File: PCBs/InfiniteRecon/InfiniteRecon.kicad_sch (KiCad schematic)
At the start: 0 parts

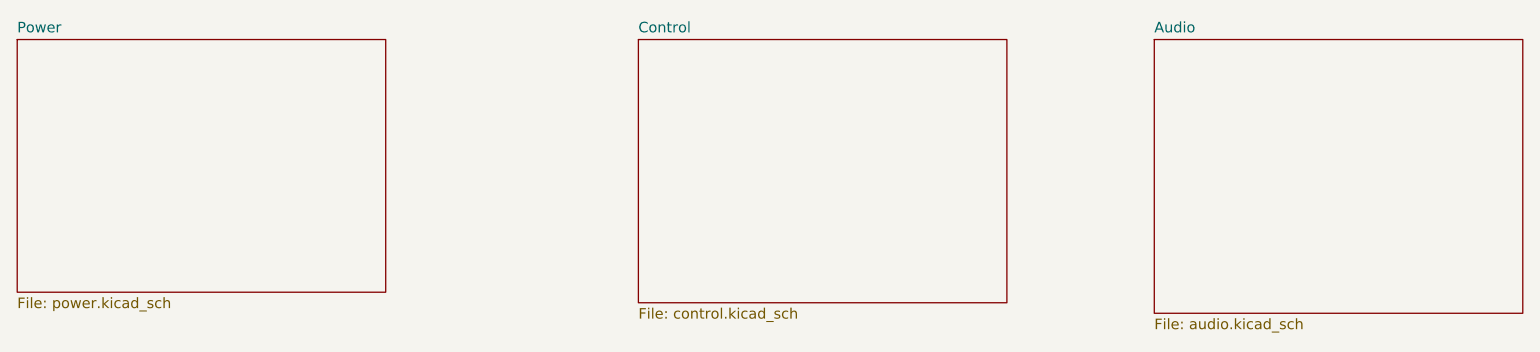
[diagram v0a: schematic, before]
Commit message: Finished Scem for the most part, awake me needs to look it over one more time
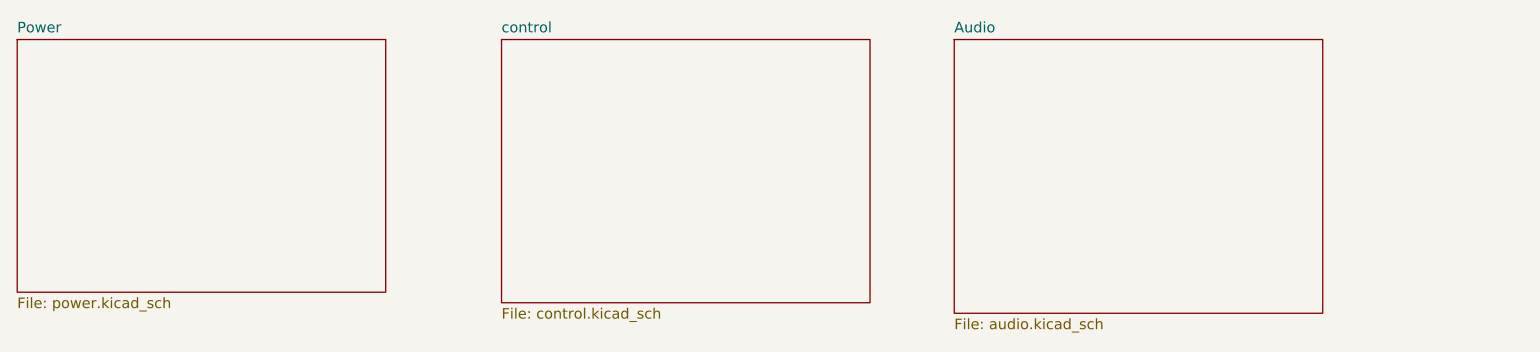
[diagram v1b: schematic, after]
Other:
- sheet Control renamed control
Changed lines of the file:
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@@
 	(title_block
 		(title "Main")
+		(date "2026-03-27")
+		(rev "1")
 	)
 	(sheet
-		(at 171.45 66.04)
+		(at 147.32 66.04)
 		(size 44.45 33.02)
 		(exclude_from_sim no)
@@
 		)
 		(property "Sheetname" "Audio"
-			(at 171.45 65.3284 0)
+			(at 147.32 65.3284 0)
 			(show_name no)
 			(do_not_autoplace no)
@@
 		)
 		(property "Sheetfile" "audio.kicad_sch"
-			(at 171.45 99.6446 0)
+			(at 147.32 99.6446 0)
 			(show_name no)
 			(do_not_autoplace no)
@@
 	)
 	(sheet
-		(at 109.22 66.04)
+		(at 92.71 66.04)
 		(size 44.45 31.75)
 		(exclude_from_sim no)
@@
 			(color 0 0 0 0)
 		)
-		(property "Sheetname" "Control"
-			(at 109.22 65.3284 0)
+		(property "Sheetname" "control"
+			(at 92.71 65.3284 0)
 			(show_name no)
 			(do_not_autoplace no)
@@
 		)
 		(property "Sheetfile" "control.kicad_sch"
-			(at 109.22 98.3746 0)
+			(at 92.71 98.3746 0)
 			(show_name no)
 			(do_not_autoplace no)
